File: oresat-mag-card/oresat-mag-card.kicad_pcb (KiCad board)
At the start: 4 copper layers, 99.8 x 94.6 mm, 234 parts, among them J1 J-SAMTEC-TFM-120-01-L-D-RA, J2 SM14B-SHLS-TF, J3 530481210, Q1 DMP2240UDM, Q2 PMV45EN, Q3 DMP3050LVT-7, Q4 DMP3050LVT-7, Q5 PMV45EN, U1 MAX7310, U10 LTC4300A-1, U11 MAX892LEUA+T, U12 STSPIN250, U13 STSPIN250, U14 INA185, U15 INA185, U16 STSPIN250, U17 INA185, U2 MIC842LYC5, U3 MIC842LYC5, U4 TS5A21366DCUR, U5 MAX4211FETE, U6 TPS62111RSA, U7 MCXN947VKLT, U8 TCAN330, U9 ICM-42688-P, Y1 24 MHz

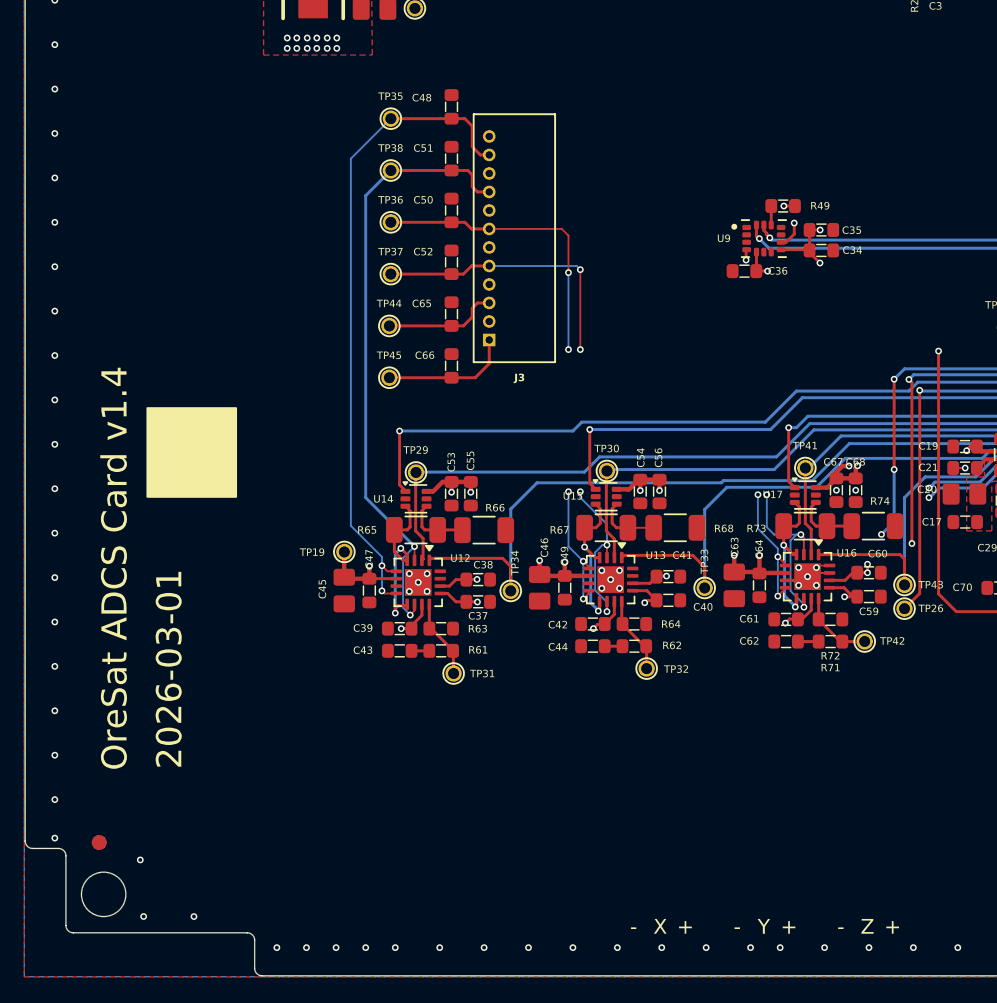
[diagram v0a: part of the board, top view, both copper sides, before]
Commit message: Update before fab!
Last final changes to pcb before fab: changed location of connector back to original. Changed silk screen to reflect date and mag board v1.0
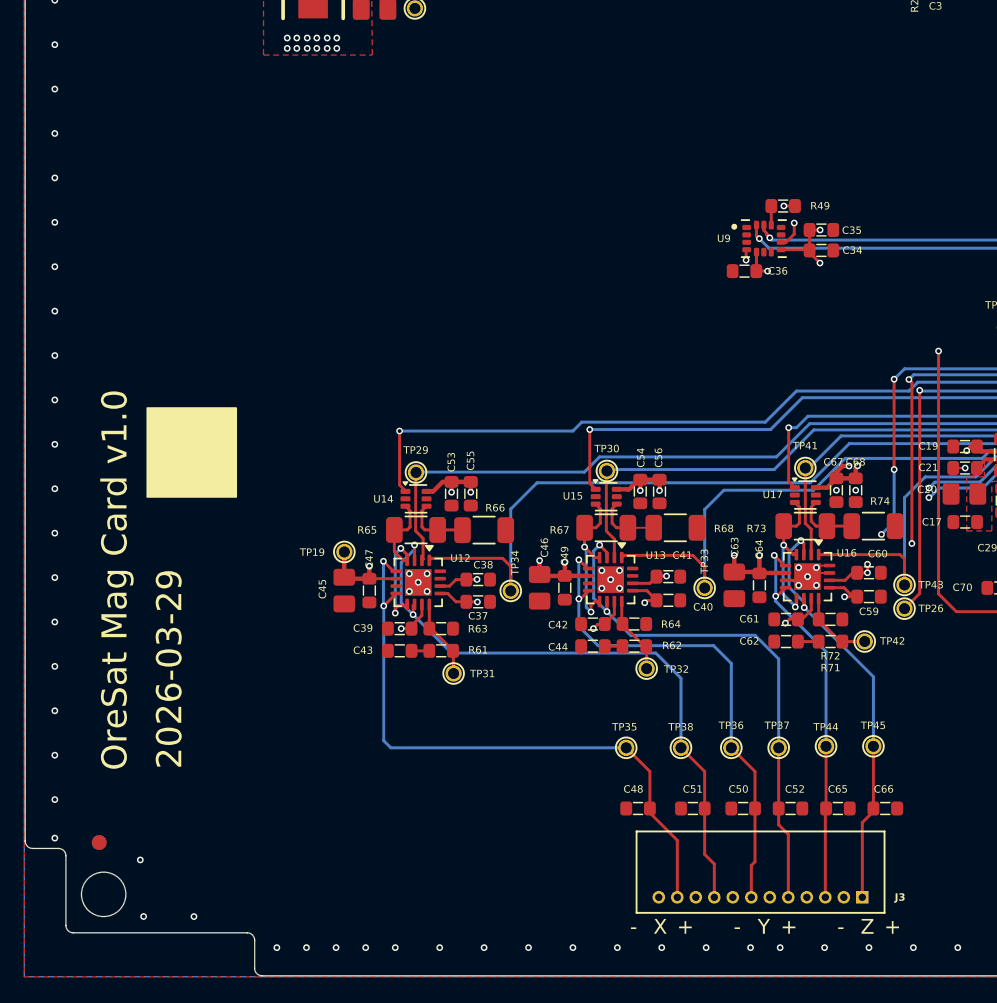
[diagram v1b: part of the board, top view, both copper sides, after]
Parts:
- moved C48 49.0 mm to (140.0, 141.0), turned to 180 degrees
- moved C51 46.8 mm to (143.7, 141.0), turned to 180 degrees
- moved TP35 45.4 mm to (139.2, 136.9), turned to -90 degrees
- moved J3 45.3 mm to (155.2, 147.0), turned to 180 degrees
- moved C50 44.9 mm to (147.1, 141.0), turned to 180 degrees
- moved TP38 43.6 mm to (142.9, 136.9), turned to -90 degrees
- moved C52 43.4 mm to (150.3, 141.0), turned to 0 degrees
- moved C65 42.4 mm to (153.5, 141.0), turned to 0 degrees
- moved TP36 42.3 mm to (146.3, 136.9), turned to -90 degrees
- moved C66 41.9 mm to (156.7, 141.0), turned to 0 degrees
- moved TP37 41.4 mm to (149.5, 136.9), turned to -90 degrees
- moved TP45 41.1 mm to (155.9, 136.8), turned to -90 degrees
- moved TP44 40.9 mm to (152.7, 136.8), turned to -90 degrees
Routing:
- net /MT_Z_OUT_B: track 48.6 -> 26.5 mm, vias 3 -> 2
- net /MT_Z_OUT_A: track 49.4 -> 28.8 mm, vias 3 -> 2
- net /MT_Y_OUT_B: track 38.7 -> 34.2 mm, vias 5 -> 2
- net /MT_Y_OUT_A: track 39.3 -> 36.1 mm, vias 5 -> 2
- net /MT_X_OUT_B: track 44.5 -> 42.6 mm
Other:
- board text added: "2026-03-29"
- board text added: "OreSat Mag Card v1.0"
- board text removed: "2023-11-21"
- board text removed: "2026-03-01"
- board text removed: "OreSat ADCS Card v1.3"
- board text removed: "OreSat ADCS Card v1.4"

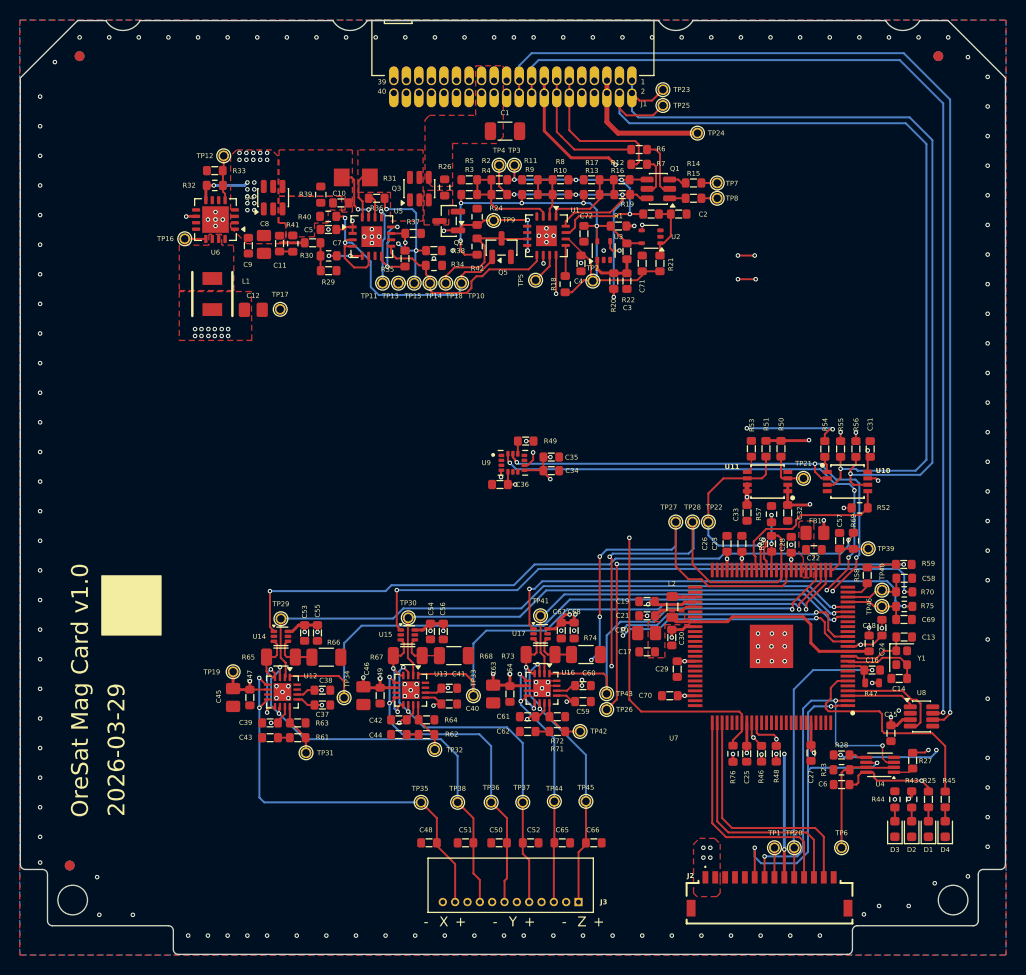
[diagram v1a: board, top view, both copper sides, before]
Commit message: Schematic polish, fixed UART TX/RX mixup, imported into layout
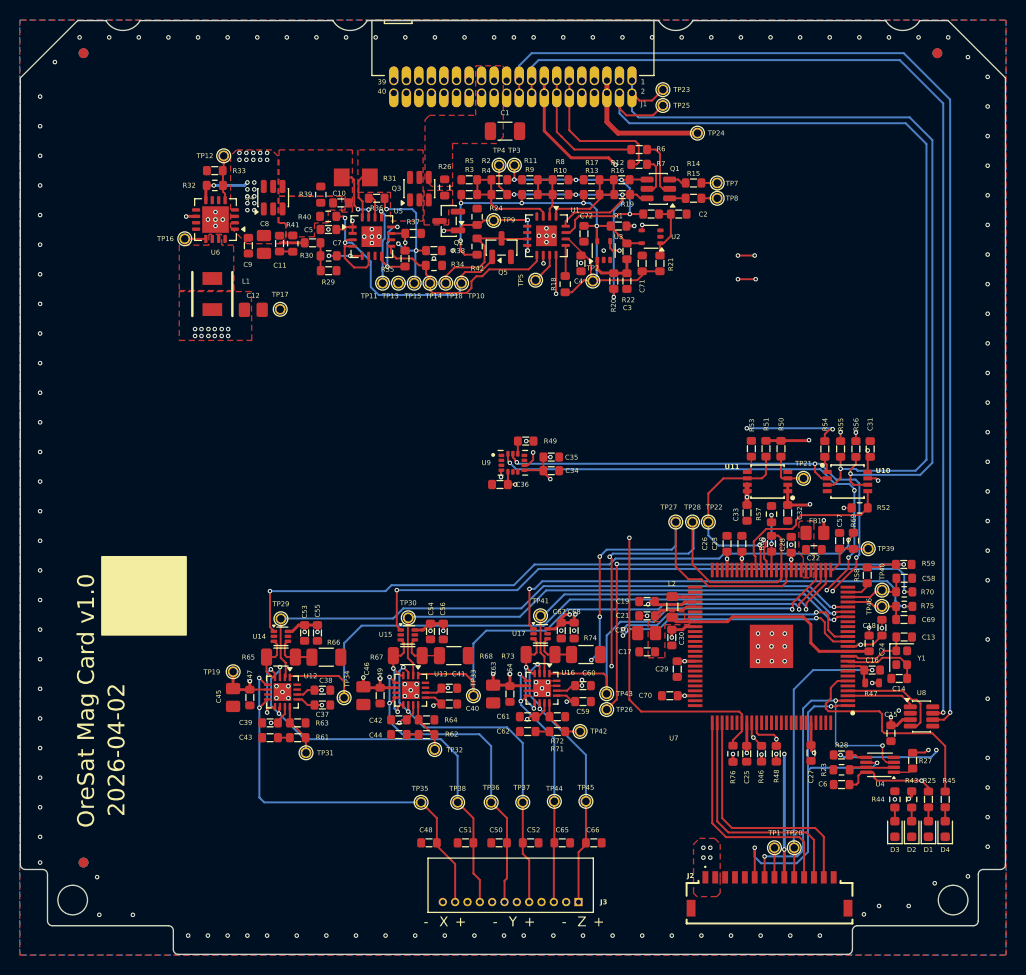
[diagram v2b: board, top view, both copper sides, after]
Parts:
- removed TP6: Test-Point, oresat-misc:TestPoint-0.75mm-th
- moved FID2 1.43 mm to (105.0, 143.0)
- moved FID4 1.43 mm to (105.0, 143.0)
- moved FID1 0.50 mm to (105.0, 61.0)
- moved FID6 0.50 mm to (105.0, 61.0)
- moved FID3 0.32 mm to (191.5, 61.0)
- moved FID5 0.32 mm to (191.5, 61.0)
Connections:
- J2 pad 6: /Card Power Domain/SW_COM1 -> /Card Power Domain/CARD-UART-TX
- J2 pad 7: /Card Power Domain/SW_COM2 -> /Card Power Domain/CARD-UART-RX
- U4 pad 2: /Card Power Domain/UART_EN -> /Card Power Domain/CARD-UART-TX
- U4 pad 3: /Card Power Domain/SW_COM2 -> /Card Power Domain/UART_EN
- U4 pad 6: /Card Power Domain/SW_COM1 -> /Card Power Domain/CARD-UART-RX
- U7 pad 1: /Card Power Domain/SW_COM1 -> /Card Power Domain/CARD-UART-RX
- U7 pad 2: /Card Power Domain/SW_COM2 -> /Card Power Domain/CARD-UART-TX
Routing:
- net /Card Power Domain/SW_COM2: track 37.3 -> 0.00 mm, vias 3 -> 0
- net /Card Power Domain/SW_COM1: track 37.0 -> 0.00 mm, vias 3 -> 0
- net (no net): track 0.00 -> 37.0 mm, vias 0 -> 3
- net /Card Power Domain/UART_EN: track 116.3 -> 145.0 mm, vias 3 -> 6
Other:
- board text added: "${ISSUE_DATE}"
- board text added: "${TITLE} v${REVISION}"

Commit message: No DRC errors
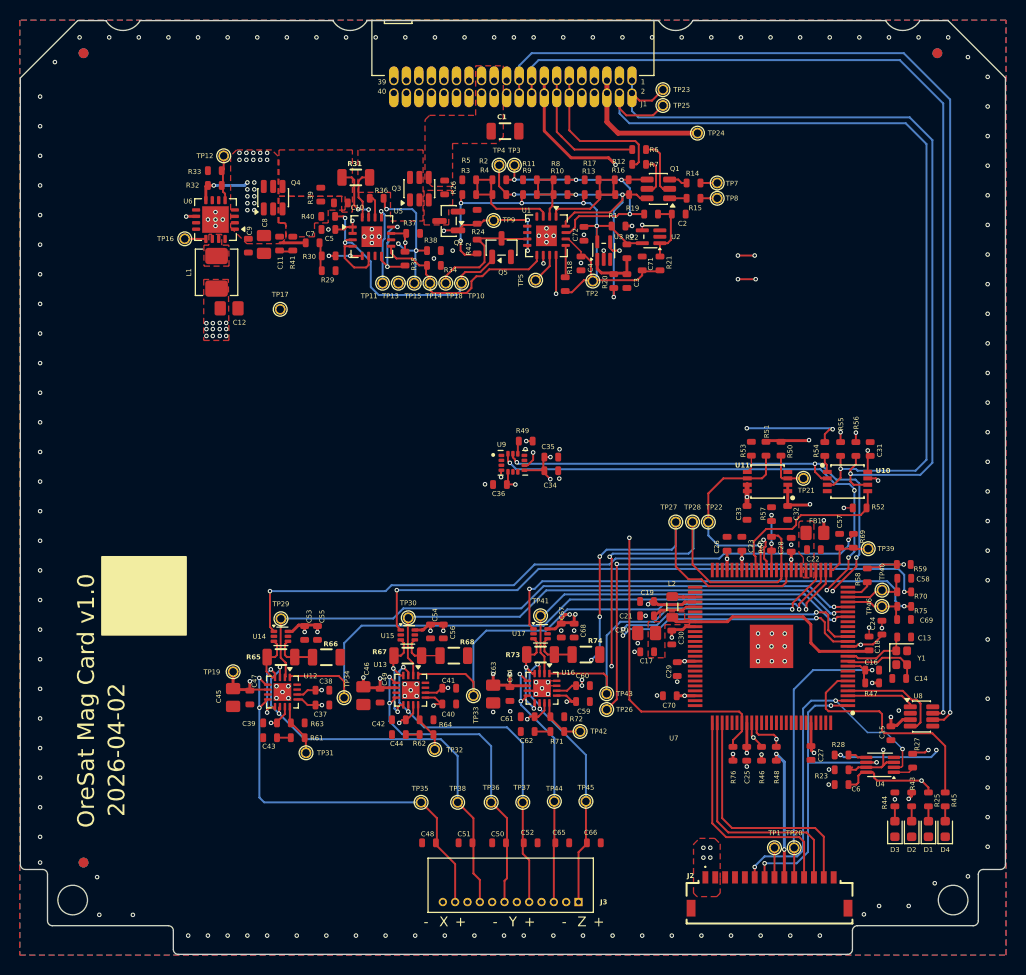
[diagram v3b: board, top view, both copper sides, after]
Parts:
- C1: footprint Capacitor_SMD:C_1206_3216Metric -> oresat-passives:1206-C
- C10, C11, C13, C14, C15, C16, C17, C18, C19, C2, C21, C22, C23, C24, C25, C26, C27, C28, C29, C3, C30, C31, C32, C33, C34, C35, C36, C37, C38, C39, C4, C40, C41, C42, C43, C44, C47, C48, C49, C5, C50, C51, C52, C53, C54, C55, C56, C57, C58, C59, C6, C60, C61, C62, C64, C65, C66, C67, C68, C69, C7, C70, C71, C72, C9, R1, R10, R11, R12, R13, R14, R15, R16, R17, R19, R2, R20, R21, R22, R25, R27, R28, R29, R3, R33, R35, R36, R37, R38, R4, R45, R46, R48, R49, R5, R50, R51, R53, R54, R55, R56, R58, R59, R6, R60, R61, R62, R63, R64, R7, R71, R72, R8, R9: footprint oresat-passives:c_0603-SMALL -> oresat-passives:0603-C-NOSILK
- J3: footprint mag-card:MOLEX_530481210 -> oresat-connectors:MOLEX_530481210
- L1: footprint oresat-acs-card:ECS-MPI4040 -> oresat-passives:L_ECS-MPI4040
- R18, R23, R24, R26, R30, R32, R34, R39, R40, R41, R42, R43, R44, R52, R57, R69, R70, R75, R76: footprint Resistor_SMD:R_0603_1608Metric -> oresat-passives:0603-C-NOSILK
- R31: footprint oresat-acs-card:R1206 -> oresat-passives:1206-C
- R65, R66, R67, R68, R73, R74: footprint Resistor_SMD:R_1206_3216Metric -> oresat-passives:1206-C
- moved C12 2.45 mm to (119.8, 86.8)
- moved L1 2.24 mm to (118.5, 83.2), turned to -90 degrees
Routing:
- net /Card Power Domain/UART_EN: track 145.0 -> 96.2 mm, vias 6 -> 4
- net /Card Power Domain/CARD-UART-TX: track 0.00 -> 37.5 mm, vias 0 -> 3
- net (no net): track 37.0 -> 0.00 mm, vias 3 -> 0
- net /Card Power Domain/CARD-UART-RX: track 0.00 -> 32.8 mm, vias 0 -> 3
- net GND: track 6.02 -> 5.21 mm, vias 167 -> 182
- net 3.3V: track 113.3 -> 113.7 mm, vias 46 -> 45
